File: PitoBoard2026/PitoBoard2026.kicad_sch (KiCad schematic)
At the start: 74 parts, among them J1 RJ25, J2 ICSP, J3 Conn_01x04_Socket, J4 Conn_01x04_Pin, SW1 RST, U1 ATmega328PB-A, U10 MCP25625-x-SS, U2 R-78E5.0-0.5, U3 MCP3425Axx-xCH, U4 SLIP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

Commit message: Add files via upload
SDP32を配置
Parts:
- removed C10: 10u, Capacitor_SMD:C_1206_3216Metric, symbol Device:C_Small
- removed C11: 2.2u, Capacitor_SMD:C_1206_3216Metric, symbol Device:C_Small
- removed C12, C13: 3.3n, Capacitor_SMD:C_1206_3216Metric, symbol Device:C_Small
- removed C6: 1u, Capacitor_SMD:C_0805_2012Metric, symbol Device:C_Small
- removed C7: 0.01u, Capacitor_SMD:C_0603_1608Metric, symbol Device:C_Small
- removed C8: 470p, Capacitor_SMD:C_0603_1608Metric, symbol Device:C_Small
- removed C9: 0.1u, Capacitor_SMD:C_0603_1608Metric, symbol Device:C_Small
- removed R19, R6: 1k, Resistor_SMD:R_0603_1608Metric, symbol Device:R_US
- removed R2, R3: 4.7k, Resistor_SMD:R_0603_1608Metric, symbol Device:R_US
- removed R4, R5: 10k, Resistor_SMD:R_0603_1608Metric, symbol Device:R_US
- removed U3: MCP3425Axx-xCH, Package_TO_SOT_SMD:SOT-23-6, symbol Analog_ADC:MCP3425Axx-xCH
- removed U5: ~, KUBTSS_parts:MPXV7002, symbol KUBTSS_parts:MPXV7002
- added C27: 100n, Capacitor_SMD:C_0603_1608Metric, symbol Device:C_Small
- added U6: SDP32, symbol KUBTSS:SDP32
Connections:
- net +5VA is gone; now on net +5V: C14.1, J4.4 (Pin_4), R11.1, R12.1, U7.1 (VDD5V)
- net +5V: now also C27.2, U6.7 (VDD)
- net GND: now also J4.1 (Pin_1), C27.1, U6.1 (GND), U6.10 (GND), U6.11 (GND), U6.2 (GND), U6.3 (GND), U6.6 (GND), U6.9 (ADDR)
- net GND1: no longer J4.1 (Pin_1)
- net SCL0: now also U6.5 (SCL)
- net SDA0: now also U6.8 (SDA)
- no-connect marks 28 -> 26
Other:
- note added: "できるだけピンの近くに配置する。"
- note removed: "2.5V"
- note removed: "MCP3425A0 → 0x68 MCP3425A1 → 0x69 MCP3425A2 → 0x6A MCP3425A3 → 0x6B （7bit アドレス表記）"
- moved on the sheet: C1, C16, C17, C18, C2, J2, R1, R13, R14, R15, R16, SW1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

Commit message: Add files via upload
フットプリント設定完了
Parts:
- removed C25, C26: 0.1u, Capacitor_SMD:C_0805_2012Metric, symbol Device:C_Small
- removed R24: 120, Resistor_SMD:R_0603_1608Metric, symbol Device:R_US
- FB1: footprint (none) -> Inductor_SMD:L_0603_1608Metric
- U11: footprint (none) -> Package_DIP:DIP-8_W7.62mm
- U6: footprint (none) -> KUBTSS:SDP32
- U9: footprint KUBTSS_parts:Temp_AE-BME280 -> KUBTSS:BME280
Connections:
- net +5V: now also U11.５ (OE)
- no-connect marks 26 -> 29
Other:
- note added: "R5をはがす"
- note added: "裏面のパッド（PCBエディターでパッド17、18）はGNDにする。"
- moved on the sheet: J2, R20, R21, R22, R23, U11

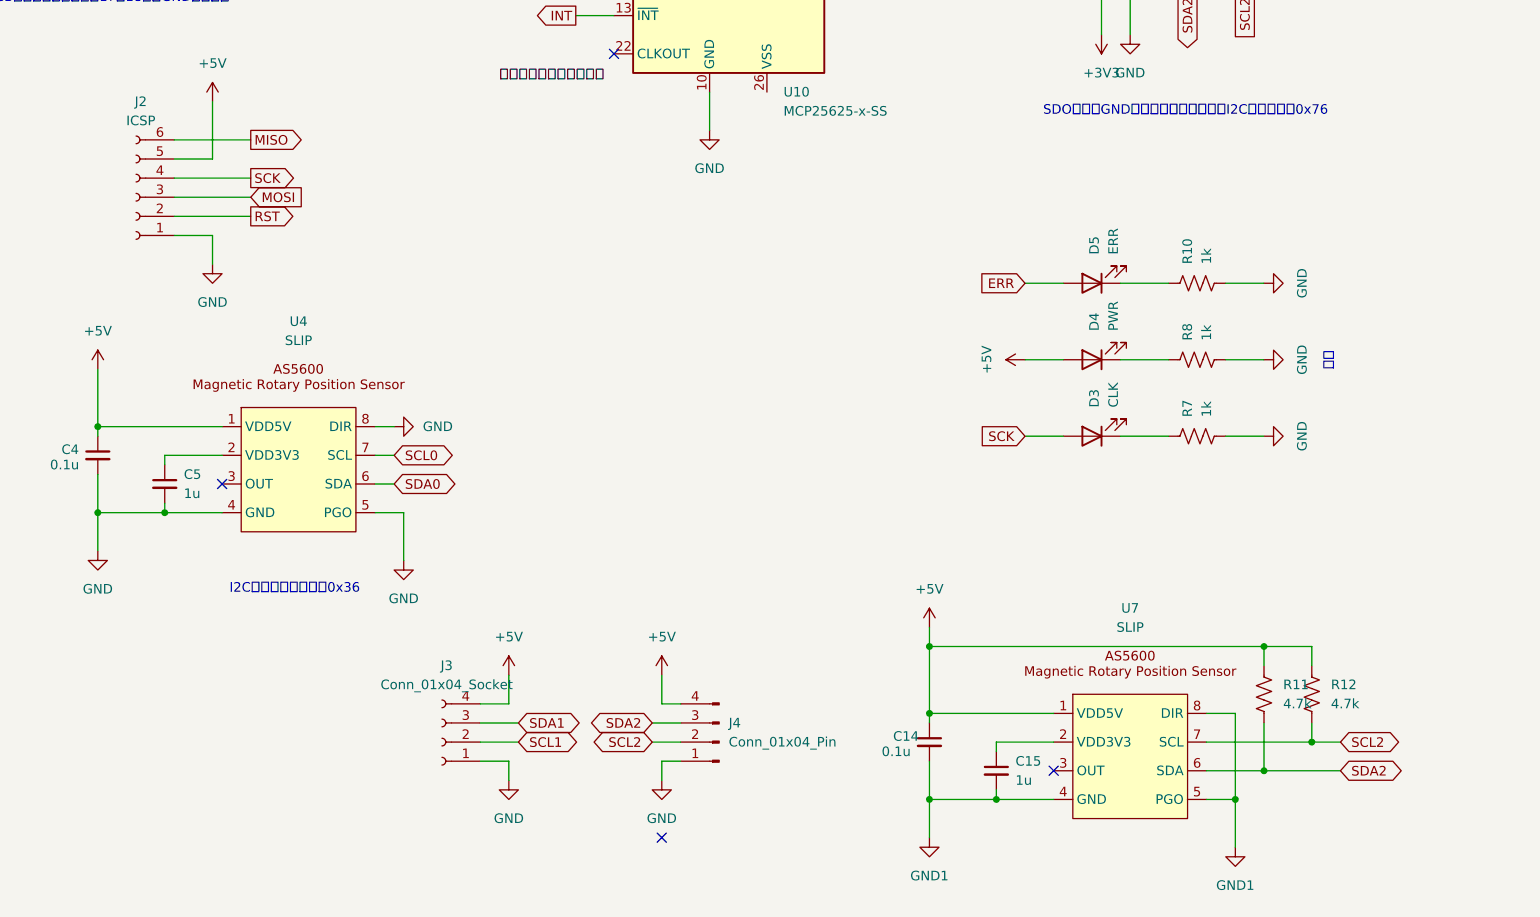
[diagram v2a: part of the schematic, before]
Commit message: I2Cのエラーを修正
5Vを3.3Vの方につないでいたのを修正
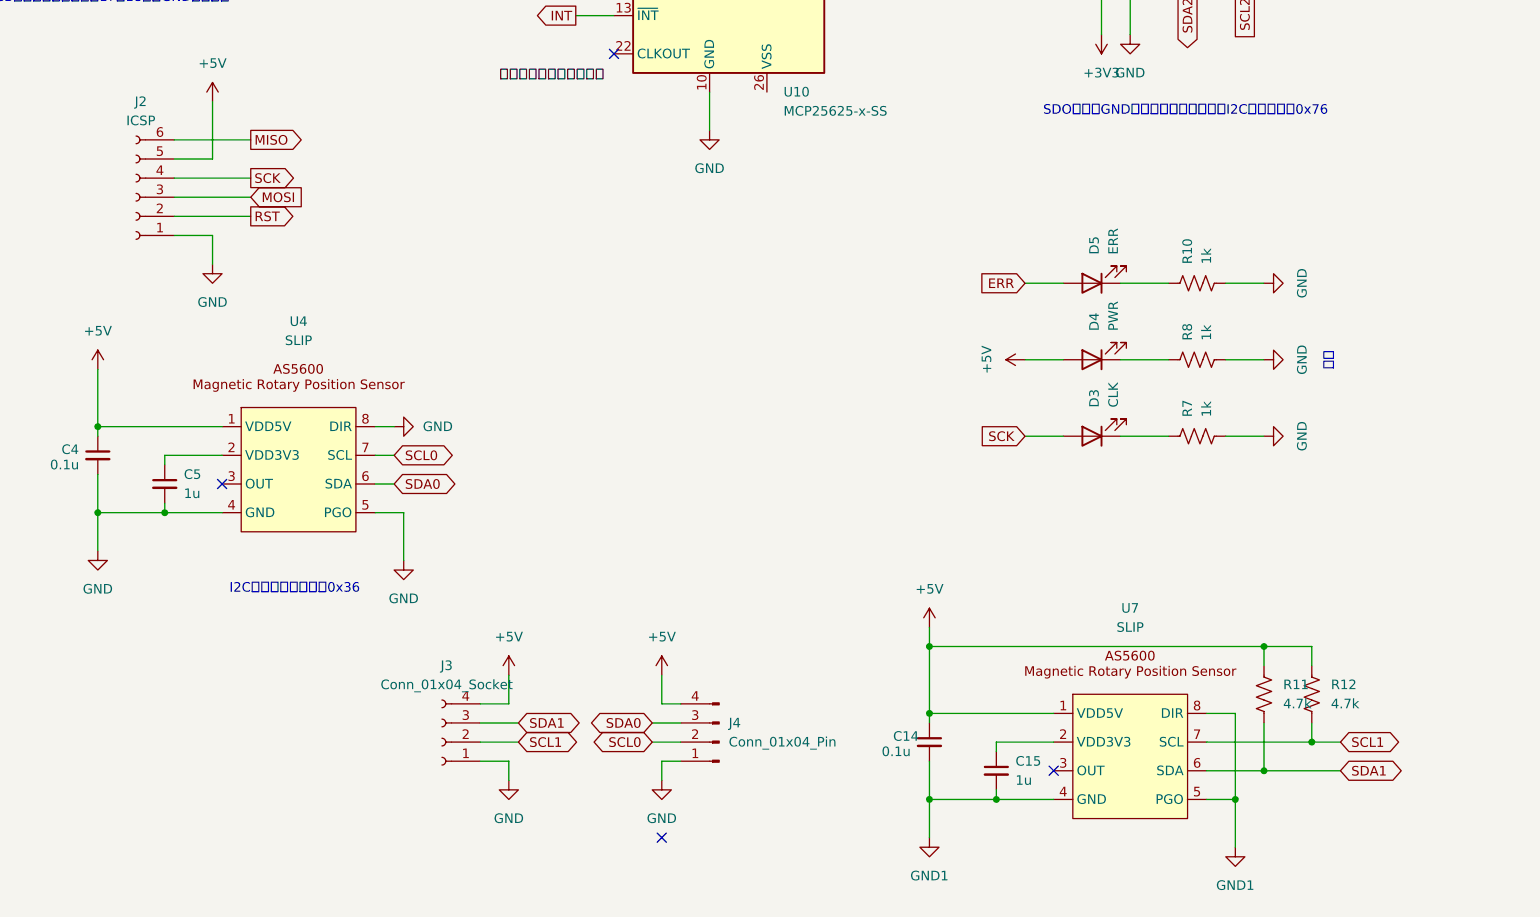
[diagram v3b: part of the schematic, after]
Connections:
- net SCL0: now also J4.2 (Pin_2)
- net SCL1: now also R12.2, U7.7 (SCL)
- net SCL2: no longer J4.2 (Pin_2), R12.2, U7.7 (SCL)
- net SDA0: now also J4.3 (Pin_3)
- net SDA1: now also R11.2, U7.6 (SDA)
- net SDA2: no longer J4.3 (Pin_3), R11.2, U7.6 (SDA)
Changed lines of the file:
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@@
 (kicad_sch
-	(version 20231120)
+	(version 20250114)
 	(generator "eeschema")
-	(generator_version "8.0")
+	(generator_version "9.0")
 	(paper "A4")
+	(text "I2Cアドレスは固定で0x36"
+		(exclude_from_sim no)
+		(at 139.192 149.86 0)
+		(effects
+			(font
+				(size 1.27 1.27)
+			)
+		)
+	)
+	(text "裏面のパッド（PCBエディターでパッド17、18）はGNDにする。"
+		(exclude_from_sim no)
+		(at 109.982 71.374 0)
+		(effects
+			(font
+				(size 1.27 1.27)
+			)
+		)
+	)
+	(text "導通"
+		(exclude_from_sim no)
+		(at 276.606 119.634 90)
+		(effects
+			(font
+				(size 1.27 1.27)
+			)
+		)
+	)
+	(text "できるだけピンの近くに配置する。"
+		(exclude_from_sim no)
+		(at 127.762 20.828 0)
+		(effects
+			(font
+				(size 1.27 1.27)
+			)
+		)
+	)
+	(text "こっちにTWIの2系統目があるので\nAS5600二つをI2C駆動してもよい"
+		(exclude_from_sim no)
+		(at 2.54 171.958 0)
+		(effects
+			(font
+				(size 1.27 1.27)
+			)
+		)
+	)
+	(text "0.125W\n"
+		(exclude_from_sim no)
+		(at 233.426 35.306 0)
+		(effects
+			(font
+				(size 1.27 1.27)
+			)
+		)
+	)
+	(text "R5をはがす\n"
+		(exclude_from_sim no)
+		(at 318.008 72.136 0)
+		(effects
+			(font
+				(size 1.27 1.27)
+			)
+		)
+	)
+	(text "SDOピンをGNDに接続しているため、I2Cアドレスは0x76"
+		(exclude_from_sim no)
+		(at 257.556 86.36 0)
+		(effects
+			(font
+				(size 1.27 1.27)
+			)
+		)
+	)
 	(junction
 		(at 307.34 60.96)
@@
 		)
 	)
-	(text "I2Cアドレスは固定で0x36"
-		(exclude_from_sim no)
-		(at 139.192 149.86 0)
-		(effects
-			(font
-				(size 1.27 1.27)
-			)
-		)
-	)
-	(text "裏面のパッド（PCBエディターでパッド17、18）はGNDにする。"
-		(exclude_from_sim no)
-		(at 109.982 71.374 0)
-		(effects
-			(font
-				(size 1.27 1.27)
-			)
-		)
-	)
-	(text "導通"
-		(exclude_from_sim no)
-		(at 276.606 119.634 90)
-		(effects
-			(font
-				(size 1.27 1.27)
-			)
-		)
-	)
-	(text "できるだけピンの近くに配置する。"
-		(exclude_from_sim no)
-		(at 127.762 20.828 0)
-		(effects
-			(font
-				(size 1.27 1.27)
-			)
-		)
-	)
-	(text "こっちにTWIの2系統目があるので\nAS5600二つをI2C駆動してもよい"
-		(exclude_from_sim no)
-		(at 2.54 171.958 0)
-		(effects
-			(font
-				(size 1.27 1.27)
-			)
-		)
-	)
-	(text "0.125W\n"
-		(exclude_from_sim no)
-		(at 233.426 35.306 0)
-		(effects
-			(font
-				(size 1.27 1.27)
-			)
-		)
-	)
-	(text "R5をはがす\n"
-		(exclude_from_sim no)
-		(at 318.008 72.136 0)
-		(effects
-			(font
-				(size 1.27 1.27)
-			)
-		)
-	)
-	(text "SDOピンをGNDに接続しているため、I2Cアドレスは0x76"
-		(exclude_from_sim no)
-		(at 257.556 86.36 0)
-		(effects
-			(font
-				(size 1.27 1.27)
-			)
-		)
-	)
 	(label "low接続で通常モード"
 		(at 167.64 30.48 0)
-		(fields_autoplaced yes)
 		(effects
 			(font
@@
 	(label "SDOピンGND接続で0x76, VDD接続で0x77"
 		(at 238.76 46.99 0)
-		(fields_autoplaced yes)
 		(effects
 			(font
@@
 	(label "内部クロックは使わない"
 		(at 166.37 82.55 0)
-		(fields_autoplaced yes)
 		(effects
 			(font
@@
 	(label "mcp25625の近くに配置する"
 		(at 212.09 54.61 0)
-		(fields_autoplaced yes)
 		(effects
 			(font
@@
 		)
 	)
-	(global_label "SCL2"
+	(global_label "SCL1"
 		(shape bidirectional)
 		(at 278.13 170.18 0)
@@
 		)
 	)
-	(global_label "SDA2"
+	(global_label "SDA1"
 		(shape bidirectional)
 		(at 278.13 173.99 0)
@@
 		)
 	)
-	(global_label "SCL2"
+	(global_label "SCL0"
 		(shape bidirectional)
 		(at 186.69 170.18 180)
@@
 		)
 	)
-	(global_label "SDA2"
+	(global_label "SDA0"
 		(shape bidirectional)
 		(at 186.69 167.64 180)
@@
 		)
 	)
+	(embedded_fonts no)
 )
